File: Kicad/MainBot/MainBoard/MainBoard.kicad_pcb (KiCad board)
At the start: 2 copper layers, 2 parts, among them U1 AZ1117-3.3, U2 Teensy3.6

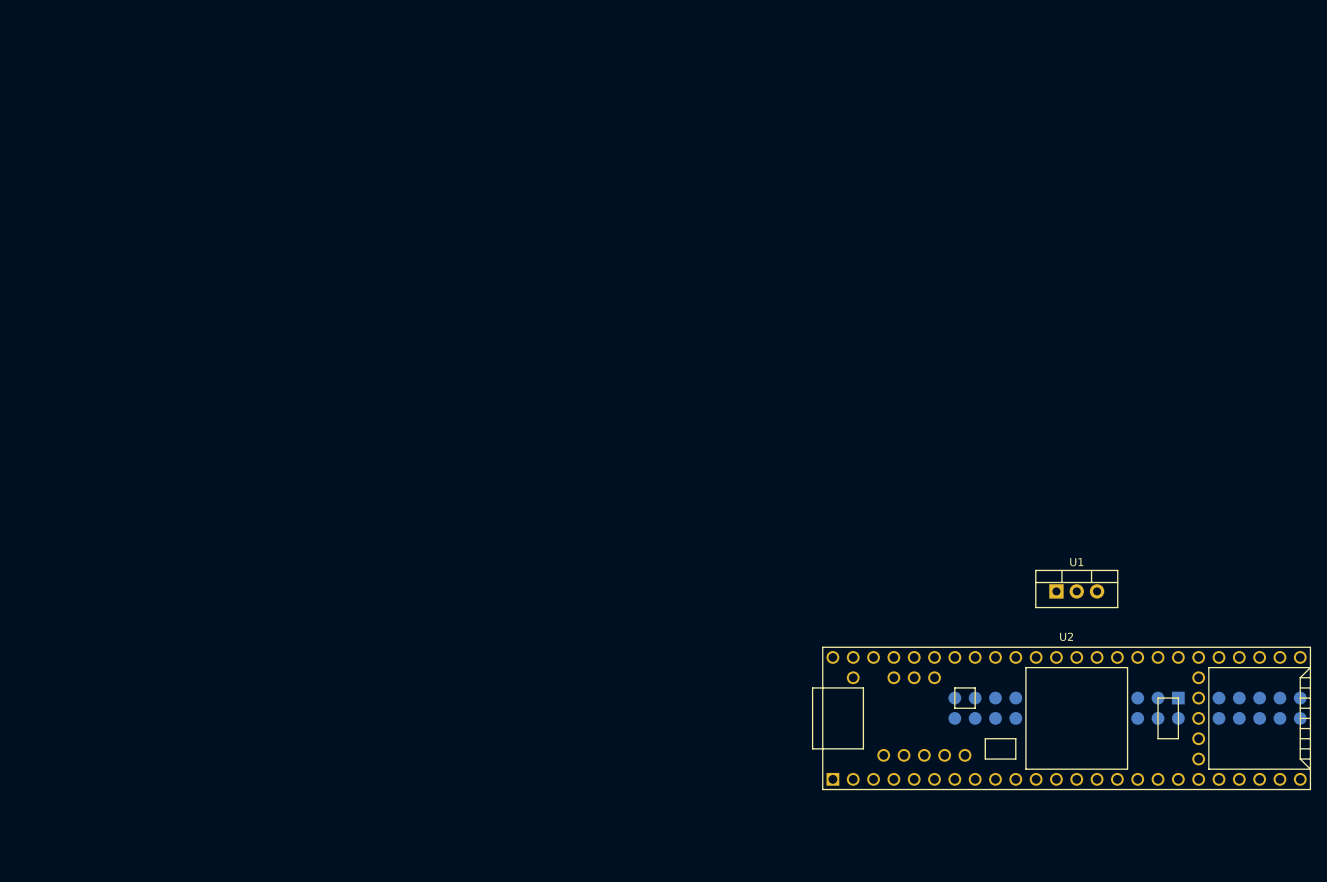
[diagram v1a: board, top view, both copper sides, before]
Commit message: Added multiplexer and driver footprint, updated PCB
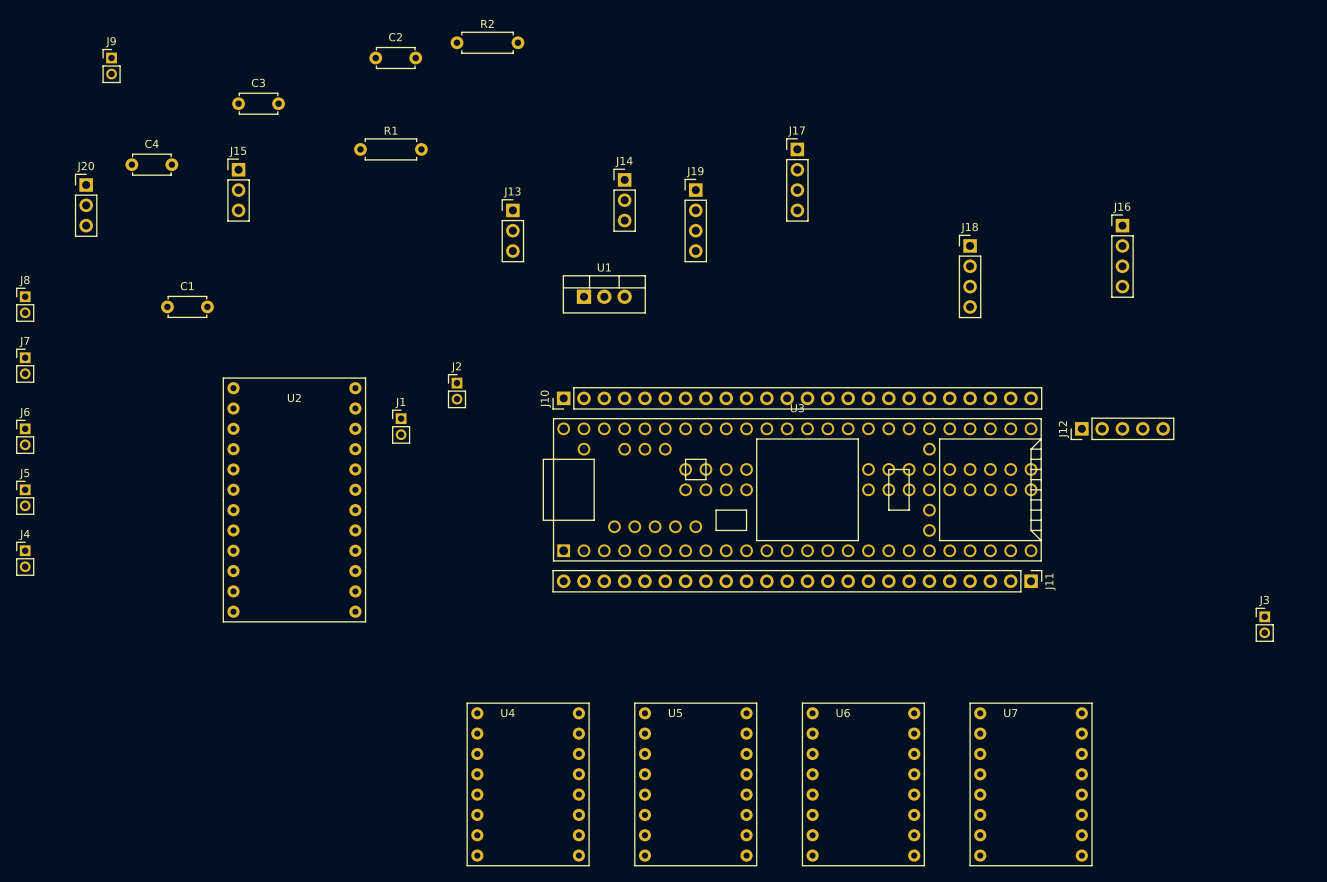
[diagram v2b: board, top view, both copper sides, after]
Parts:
- added C1: C, Capacitors_THT:C_Disc_D4.7mm_W2.5mm_P5.00mm, F.Cu at (35.6, 53.3)
- added C2: C, Capacitors_THT:C_Disc_D4.7mm_W2.5mm_P5.00mm, F.Cu at (61.6, 22.2)
- added C3: C, Capacitors_THT:C_Disc_D4.7mm_W2.5mm_P5.00mm, F.Cu at (44.5, 27.9)
- added C4: C, Capacitors_THT:C_Disc_D4.7mm_W2.5mm_P5.00mm, F.Cu at (31.1, 35.6)
- added J1: Conn_01x02, Pin_Headers:Pin_Header_Straight_1x02_Pitch2.00mm, F.Cu at (64.8, 67.3)
- added J10: Conn_01x24, Pin_Headers:Pin_Header_Straight_1x24_Pitch2.54mm, F.Cu at (85.1, 64.8)
- added J11: Conn_01x24, Pin_Headers:Pin_Header_Straight_1x24_Pitch2.54mm, F.Cu at (143.5, 87.6)
- added J12: Conn_01x05, Pin_Headers:Pin_Header_Straight_1x05_Pitch2.54mm, F.Cu at (149.9, 68.6)
- added J13: Conn_01x03, Pin_Headers:Pin_Header_Straight_1x03_Pitch2.54mm, F.Cu at (78.7, 41.3)
- added J14: Conn_01x03, Pin_Headers:Pin_Header_Straight_1x03_Pitch2.54mm, F.Cu at (92.7, 37.5)
- added J15: Conn_01x03, Pin_Headers:Pin_Header_Straight_1x03_Pitch2.54mm, F.Cu at (44.5, 36.2)
- added J16: Conn_01x04, Pin_Headers:Pin_Header_Straight_1x04_Pitch2.54mm, F.Cu at (154.9, 43.2)
- added J17: Conn_01x04, Pin_Headers:Pin_Header_Straight_1x04_Pitch2.54mm, F.Cu at (114.3, 33.7)
- added J18: Conn_01x04, Pin_Headers:Pin_Header_Straight_1x04_Pitch2.54mm, F.Cu at (135.9, 45.7)
- added J19: Conn_01x04, Pin_Headers:Pin_Header_Straight_1x04_Pitch2.54mm, F.Cu at (101.6, 38.7)
- added J2: Conn_01x02, Pin_Headers:Pin_Header_Straight_1x02_Pitch2.00mm, F.Cu at (71.8, 62.9)
- added J20: Conn_01x03, Pin_Headers:Pin_Header_Straight_1x03_Pitch2.54mm, F.Cu at (25.4, 38.1)
- added J3: Conn_01x02, Pin_Headers:Pin_Header_Straight_1x02_Pitch2.00mm, F.Cu at (172.7, 92.1)
- added J4: Conn_01x02, Pin_Headers:Pin_Header_Straight_1x02_Pitch2.00mm, F.Cu at (17.8, 83.8)
- added J5: Conn_01x02, Pin_Headers:Pin_Header_Straight_1x02_Pitch2.00mm, F.Cu at (17.8, 76.2)
- added J6: Conn_01x02, Pin_Headers:Pin_Header_Straight_1x02_Pitch2.00mm, F.Cu at (17.8, 68.6)
- added J7: Conn_01x02, Pin_Headers:Pin_Header_Straight_1x02_Pitch2.00mm, F.Cu at (17.8, 59.7)
- added J8: Conn_01x02, Pin_Headers:Pin_Header_Straight_1x02_Pitch2.00mm, F.Cu at (17.8, 52.1)
- added J9: Conn_01x02, Pin_Headers:Pin_Header_Straight_1x02_Pitch2.00mm, F.Cu at (28.6, 22.2)
- added R1: R, Resistors_THT:R_Axial_DIN0207_L6.3mm_D2.5mm_P7.62mm_Horizontal, F.Cu at (59.7, 33.7)
- added R2: R, Resistors_THT:R_Axial_DIN0207_L6.3mm_D2.5mm_P7.62mm_Horizontal, F.Cu at (71.8, 20.3)
- added U3: Teensy3.6, Teensy:Teensy35_36, F.Cu at (114.3, 76.2)
- added U4: DRV8825, Rex:DRV8825, F.Cu at (80.6, 113.0)
- added U5: DRV8825, Rex:DRV8825, F.Cu at (101.6, 113.0)
- added U6: DRV8825, Rex:DRV8825, F.Cu at (122.6, 113.0)
- added U7: DRV8825, Rex:DRV8825, F.Cu at (143.5, 113.0)
- U2: value Teensy3.6 -> TCA9548A; footprint Teensy:Teensy35_36 -> Rex:TCA9548A
- moved U2 112.0 mm to (43.8, 63.5)
- moved U1 69.6 mm to (87.6, 52.1)
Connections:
- U2 pad 1: GND -> (no net)
- U2 pad 10: Net-(U2-Pad10) -> (no net)
- U2 pad 11: Net-(U2-Pad11) -> (no net)
- U2 pad 12: Net-(U2-Pad12) -> (no net)
- U2 pad 13: Net-(U2-Pad13) -> (no net)
- U2 pad 14: Net-(U2-Pad14) -> (no net)
- U2 pad 15: Net-(U2-Pad15) -> (no net)
- U2 pad 16: Net-(U2-Pad16) -> (no net)
- U2 pad 17: Net-(U2-Pad17) -> (no net)
- U2 pad 18: Net-(U2-Pad18) -> (no net)
- U2 pad 19: Net-(U2-Pad19) -> (no net)
- U2 pad 2: Net-(U2-Pad2) -> (no net)
- U2 pad 20: Net-(U2-Pad20) -> (no net)
- U2 pad 21: Net-(U2-Pad21) -> (no net)
- U2 pad 22: Net-(U2-Pad22) -> (no net)
- U2 pad 23: Net-(U2-Pad23) -> (no net)
- U2 pad 24: Net-(U2-Pad24) -> (no net)
- U2 pad 3: Net-(U2-Pad3) -> (no net)
- U2 pad 4: /PWM_1 -> (no net)
- U2 pad 5: /PWM_2 -> (no net)
- U2 pad 6: /PWM_3 -> (no net)
- U2 pad 7: /PWM_4 -> (no net)
- U2 pad 8: Net-(U2-Pad8) -> (no net)
- U2 pad 9: Net-(U2-Pad9) -> (no net)

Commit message: Corrections and started PCB
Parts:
- added C10: 10µF, Capacitors_SMD:CP_Elec_8x5.4, F.Cu at (74.0, 136.8)
- added C11: 10µF, Capacitors_SMD:CP_Elec_8x5.4, F.Cu at (85.4, 136.8)
- added C12: 10µF, Capacitors_SMD:CP_Elec_8x5.4, F.Cu at (85.4, 126.0)
- added C13: 100µF, Capacitors_THT:CP_Radial_D6.3mm_P2.50mm, F.Cu at (200.7, 134.6)
- added C14: 100µF, Capacitors_THT:CP_Radial_D6.3mm_P2.50mm, F.Cu at (246.4, 135.9)
- added C15: 100µF, Capacitors_THT:CP_Radial_D6.3mm_P2.50mm, F.Cu at (273.1, 135.9)
- added C16: 100µF, Capacitors_THT:CP_Radial_D6.3mm_P2.50mm, F.Cu at (224.8, 134.6)
- added C5: 27pF, Capacitors_SMD:C_1206_HandSoldering, F.Cu at (123.2, 43.2)
- added C6: 10µF, Capacitors_SMD:CP_Elec_8x5.4, F.Cu at (74.0, 158.4)
- added C7: 10µF, Capacitors_SMD:CP_Elec_8x5.4, F.Cu at (85.4, 147.6)
- added C8: 10µF, Capacitors_SMD:CP_Elec_8x5.4, F.Cu at (85.4, 158.4)
- added C9: 10µF, Capacitors_SMD:CP_Elec_8x5.4, F.Cu at (74.0, 147.6)
- added D1: LED, LEDs:LED_1206, F.Cu at (162.6, 86.4)
- added D2: LED, LEDs:LED_1206, F.Cu at (162.6, 91.4)
- added D3: LED, LEDs:LED_1206, F.Cu at (162.6, 96.5)
- added J21: Conn_01x03, Pin_Headers:Pin_Header_Straight_1x03_Pitch2.54mm, F.Cu at (166.4, 133.3)
- added J22: Conn_01x03, Pin_Headers:Pin_Header_Straight_1x03_Pitch2.54mm, F.Cu at (172.7, 110.5)
- added J23: 01x04, Pin_Headers:Pin_Header_Straight_1x04_Pitch2.54mm, F.Cu at (217.2, 63.5)
- added J24: 01x03, Pin_Headers:Pin_Header_Straight_1x03_Pitch2.54mm, F.Cu at (177.8, 110.5)
- added J25: Conn_01x04, Pin_Headers:Pin_Header_Straight_1x04_Pitch2.54mm, F.Cu at (166.4, 120.7)
- added J26: 01x04, Pin_Headers:Pin_Header_Straight_1x04_Pitch2.54mm, F.Cu at (163.8, 24.1)
- added J27: Conn_01x02, Pin_Headers:Pin_Header_Straight_1x02_Pitch2.54mm, F.Cu at (172.7, 102.9)
- added J28: Conn_02x03_Counter_Clockwise, Pin_Headers:Pin_Header_Straight_2x03_Pitch2.54mm, F.Cu at (174.0, 133.3)
- added J29: Conn_02x03_Counter_Clockwise, Pin_Headers:Pin_Header_Straight_2x03_Pitch2.54mm, F.Cu at (161.3, 52.1)
- added J30: Conn_02x03_Counter_Clockwise, Pin_Headers:Pin_Header_Straight_2x03_Pitch2.54mm, F.Cu at (146.1, 133.3)
- added J31: Conn_02x03_Counter_Clockwise, Pin_Headers:Pin_Header_Straight_2x03_Pitch2.54mm, F.Cu at (153.7, 133.3)
- added J32: Conn_01x03, Connectors_JST:JST_XH_B03B-XH-A_03x2.50mm_Straight, F.Cu at (145.5, 112.8)
- added J33: Conn_01x03, Connectors_JST:JST_XH_B03B-XH-A_03x2.50mm_Straight, F.Cu at (146.1, 88.4)
- added J34: Conn_01x02, Pin_Headers:Pin_Header_Straight_1x02_Pitch2.54mm, F.Cu at (177.8, 102.9)
- added J35: Conn_01x02, Pin_Headers:Pin_Header_Straight_1x02_Pitch2.54mm, F.Cu at (182.9, 102.9)
- added J36: Conn_01x02, Pin_Headers:Pin_Header_Straight_1x02_Pitch2.54mm, F.Cu at (188.0, 102.9)
- added J37: Conn_01x02, Pin_Headers:Pin_Header_Straight_1x02_Pitch2.54mm, F.Cu at (157.5, 102.9)
- added J38: Conn_01x03, Connectors_JST:JST_XH_B03B-XH-A_03x2.50mm_Straight, F.Cu at (145.8, 96.5)
- added J39: Conn_01x04, Connectors_JST:JST_XH_B04B-XH-A_04x2.50mm_Straight, F.Cu at (232.4, 154.9)
- added J40: Conn_01x03, Connectors_JST:JST_XH_B03B-XH-A_03x2.50mm_Straight, F.Cu at (145.8, 104.6)
- added J41: 01x04, Connectors_JST:JST_XH_B04B-XH-A_04x2.50mm_Straight, F.Cu at (196.8, 146.1)
- added J42: 01x04, Connectors_JST:JST_XH_B04B-XH-A_04x2.50mm_Straight, F.Cu at (221.0, 144.8)
- added J43: 01x04, Connectors_JST:JST_XH_B04B-XH-A_04x2.50mm_Straight, F.Cu at (242.6, 144.8)
- added J44: 01x04, Connectors_JST:JST_XH_B04B-XH-A_04x2.50mm_Straight, F.Cu at (269.2, 144.8)
- added L1: 22µH, Rex:L1, F.Cu at (93.7, 129.9)
- added Q1: Q_PMOS_DGS, TO_SOT_Packages_SMD:SOT-23, F.Cu at (103.8, 152.7)
- added R10: 2.55k, Resistors_SMD:R_0805_HandSoldering, F.Cu at (15.9, 62.9)
- added R11: 2.55k, Resistors_SMD:R_0805_HandSoldering, F.Cu at (25.4, 65.4)
- added R12: 2.55k, Resistors_SMD:R_0805_HandSoldering, F.Cu at (15.2, 48.3)
- added R13: 2.55k, Resistors_SMD:R_0805_HandSoldering, F.Cu at (25.4, 50.8)
- added R14: 2.55k, Resistors_SMD:R_0805_HandSoldering, F.Cu at (15.2, 33.7)
- added R15: 2.55k, Resistors_SMD:R_0805_HandSoldering, F.Cu at (25.4, 36.2)
- added R16: 2.55k, Resistors_SMD:R_0805_HandSoldering, F.Cu at (15.2, 19.1)
- added R17: 2.55k, Resistors_SMD:R_0805_HandSoldering, F.Cu at (25.4, 21.6)
- added R18: 2.55k, Resistors_SMD:R_0805_HandSoldering, F.Cu at (57.1, 47.6)
- added R19: 2.55k, Resistors_SMD:R_0805_HandSoldering, F.Cu at (57.1, 45.7)
- added R20: 100k, Resistors_SMD:R_1206_HandSoldering, F.Cu at (57.8, 43.2)
- added R21: 100k, Resistors_SMD:R_1206_HandSoldering, F.Cu at (97.5, 148.3)
- added R22: 100k, Resistors_SMD:R_1206_HandSoldering, F.Cu at (103.2, 156.5)
- added R23: 100k, Resistors_SMD:R_1206_HandSoldering, F.Cu at (93.0, 159.7)
- added R24: 22.1k, Resistors_SMD:R_1206_HandSoldering, F.Cu at (93.0, 152.7)
- added R25: 2k, Resistors_SMD:R_1206_HandSoldering, F.Cu at (82.5, 111.8)
- added R26: 2k, Resistors_SMD:R_1206_HandSoldering, F.Cu at (82.5, 106.7)
- added R3: 2.55k, Resistors_SMD:R_0805_HandSoldering, F.Cu at (41.3, 65.4)
- added R4: 2.55k, Resistors_SMD:R_0805_HandSoldering, F.Cu at (41.3, 50.8)
- added R5: 2.55k, Resistors_SMD:R_0805_HandSoldering, F.Cu at (31.1, 48.3)
- added R6: 2.55k, Resistors_SMD:R_0805_HandSoldering, F.Cu at (31.1, 33.7)
- added R7: 2.55k, Resistors_SMD:R_0805_HandSoldering, F.Cu at (41.3, 36.2)
- added R8: 2.55k, Resistors_SMD:R_0805_HandSoldering, F.Cu at (31.1, 19.1)
- added R9: 2.55k, Resistors_SMD:R_0805_HandSoldering, F.Cu at (41.3, 22.2)
- C1, C3: value C -> 100nF; footprint Capacitors_THT:C_Disc_D4.7mm_W2.5mm_P5.00mm -> Capacitors_SMD:C_1206_HandSoldering
- C2: value C -> 4.7µF; footprint Capacitors_THT:C_Disc_D4.7mm_W2.5mm_P5.00mm -> Capacitors_SMD:C_1206_HandSoldering
- C4: value C -> 1µF; footprint Capacitors_THT:C_Disc_D4.7mm_W2.5mm_P5.00mm -> Capacitors_SMD:C_1206_HandSoldering
- J1, J2, J3, J4, J8, J9: value Conn_01x02 -> Conn_01x04; footprint Pin_Headers:Pin_Header_Straight_1x02_Pitch2.00mm -> Connectors_JST:JST_XH_B04B-XH-A_04x2.50mm_Straight
- J10, J11: value Conn_01x24 -> Conn_01x04; footprint Pin_Headers:Pin_Header_Straight_1x24_Pitch2.54mm -> Connectors_JST:JST_XH_B04B-XH-A_04x2.50mm_Straight
- J12: value Conn_01x05 -> Conn_01x04; footprint Pin_Headers:Pin_Header_Straight_1x05_Pitch2.54mm -> Connectors_JST:JST_XH_B04B-XH-A_04x2.50mm_Straight
- J13: value Conn_01x03 -> 01x02_DAC; footprint Pin_Headers:Pin_Header_Straight_1x03_Pitch2.54mm -> Pin_Headers:Pin_Header_Straight_1x02_Pitch2.54mm
- J14: value Conn_01x03 -> 01x02; footprint Pin_Headers:Pin_Header_Straight_1x03_Pitch2.54mm -> Pin_Headers:Pin_Header_Straight_1x02_Pitch2.54mm
- J15: value Conn_01x03 -> Conn_01x24; footprint Pin_Headers:Pin_Header_Straight_1x03_Pitch2.54mm -> Socket_Strips:Socket_Strip_Straight_1x24_Pitch2.54mm
- J16: value Conn_01x04 -> Conn_01x24; footprint Pin_Headers:Pin_Header_Straight_1x04_Pitch2.54mm -> Socket_Strips:Socket_Strip_Straight_1x24_Pitch2.54mm
- J17, J18: value Conn_01x04 -> 01x24; footprint Pin_Headers:Pin_Header_Straight_1x04_Pitch2.54mm -> Socket_Strips:Socket_Strip_Straight_1x24_Pitch2.54mm
- J19: value Conn_01x04 -> 01x05; footprint Pin_Headers:Pin_Header_Straight_1x04_Pitch2.54mm -> Pin_Headers:Pin_Header_Straight_1x05_Pitch2.54mm
- J20: value Conn_01x03 -> 01x03
- J5: value Conn_01x02 -> 02x04_I2C; footprint Pin_Headers:Pin_Header_Straight_1x02_Pitch2.00mm -> Pin_Headers:Pin_Header_Straight_2x04_Pitch2.54mm
- J6, J7: value Conn_01x02 -> 02x03; footprint Pin_Headers:Pin_Header_Straight_1x02_Pitch2.00mm -> Pin_Headers:Pin_Header_Straight_2x03_Pitch2.54mm
- R1: value R -> 2k; footprint Resistors_THT:R_Axial_DIN0207_L6.3mm_D2.5mm_P7.62mm_Horizontal -> Resistors_SMD:R_1206_HandSoldering
- R2: value R -> 2.55k; footprint Resistors_THT:R_Axial_DIN0207_L6.3mm_D2.5mm_P7.62mm_Horizontal -> Resistors_SMD:R_0805_HandSoldering
- U1: value AZ1117-3.3 -> TCA9548A; footprint TO_SOT_Packages_THT:TO-220-3_Vertical -> Rex:TCA9548A_TSSOP
- U2: value TCA9548A -> ISL85410; footprint Rex:TCA9548A -> DFN-12_DE-M:DFN-12_DE-M
- moved J20 165.9 mm to (161.3, 133.3)
- moved J17 164.4 mm to (260.4, 109.2), turned to 270 degrees
- moved J15 162.2 mm to (201.9, 74.9), turned to 90 degrees
- moved J5 160.3 mm to (175.8, 49.3)
- moved J3 158.3 mm to (21.0, 47.0), turned to 270 degrees
- moved C4 139.6 mm to (97.5, 158.4), turned to 270 degrees
- moved J18 138.0 mm to (260.4, 105.4), turned to 270 degrees
- moved J7 136.1 mm to (153.7, 52.1)
- moved C3 132.8 mm to (103.2, 147.0), turned to 90 degrees
- moved U7 130.8 mm to (273.1, 130.8)
- moved J6 129.3 mm to (146.1, 52.1)
- moved C2 128.6 mm to (97.5, 145.7), turned to 180 degrees
- moved J11 127.5 mm to (36.8, 17.8)
- moved U6 125.1 mm to (246.4, 130.8)
- moved U5 124.5 mm to (224.8, 130.8)
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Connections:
- C1 pad 1: GND -> /A13
- C1 pad 2: Net-(C1-Pad2) -> GND
- C2 pad 1: GND -> +12C
- C2 pad 2: Net-(C2-Pad2) -> GND
- C3 pad 1: GND -> Net-(C3-Pad1)
- C4 pad 1: GND -> Net-(C4-Pad1)
- C4 pad 2: +12V -> GND
- J1 pad 1: /TX_1 -> VCC
- J1 pad 2: /RX_1 -> /M_SC0
- J10 pad 1: /Vin -> VCC
- J10 pad 2: /AGND -> /M_SC5
- J10 pad 3: VCC -> /M_SD5
- J10 pad 4: /PWM_15 -> GND
- J11 pad 1: Net-(J11-Pad1) -> VCC
- J11 pad 2: Net-(J11-Pad2) -> /M_SC4
- J11 pad 3: /PWM_11 -> /M_SD4
- J11 pad 4: /PWM_10 -> GND
- J12 pad 1: Net-(J12-Pad1) -> VCC
- J12 pad 2: Net-(J12-Pad2) -> /TX2
- J12 pad 3: GND -> /RX2
- J12 pad 4: Net-(J12-Pad4) -> GND
- J13 pad 1: /DC_DIR_1 -> /A21
- J13 pad 2: /DC_PWM_1 -> /A22
- J14 pad 1: /DC_DIR_2 -> +12C
- J14 pad 2: /DC_PWM_2 -> GND
- J15 pad 1: /DC_DIR_3 -> /Vin
- J15 pad 2: /DC_PWM_3 -> GND
- J15 pad 3: GND -> VCC
- J16 pad 1: Net-(J16-Pad1) -> /Vin
- J16 pad 2: Net-(J16-Pad2) -> GND
- J16 pad 3: Net-(J16-Pad3) -> VCC
- J16 pad 4: Net-(J16-Pad4) -> /A9
- J17 pad 1: Net-(J17-Pad1) -> /A13
- J17 pad 2: Net-(J17-Pad2) -> /A12
- J17 pad 3: Net-(J17-Pad3) -> /PWM_11
- J17 pad 4: Net-(J17-Pad4) -> /PWM_10
- J18 pad 1: Net-(J18-Pad1) -> /A13
- J18 pad 2: Net-(J18-Pad2) -> /A12
- J18 pad 3: Net-(J18-Pad3) -> /PWM_11
- J18 pad 4: Net-(J18-Pad4) -> /PWM_10
- J19 pad 3: Net-(J19-Pad3) -> GND
- J19 pad 4: Net-(J19-Pad4) -> VCC
- J2 pad 1: /M_SD0 -> VCC
- J2 pad 2: /M_SC0 -> /M_SC1
- J20 pad 1: /DC_DIR_4 -> Net-(J20-Pad1)
- J20 pad 2: /DC_PWM_4 -> Net-(J20-Pad2)
- J20 pad 3: GND -> Net-(J20-Pad3)
- J3 pad 1: /M_SD1 -> VCC
- J3 pad 2: /M_SC1 -> /M_SC2
- J4 pad 1: /M_SD2 -> VCC
- J4 pad 2: /M_SC2 -> /M_SC3
- J5 pad 1: /M_SD3 -> /A19
- J5 pad 2: /M_SC3 -> /SCA1
- J6 pad 1: /M_SD4 -> /MISO1
- J6 pad 2: /M_SC4 -> /A13
- J7 pad 1: /M_SD5 -> /MISO2
- J7 pad 2: /M_SC5 -> /SCK2
- J8 pad 1: /M_SD6 -> VCC
- J8 pad 2: /M_SC6 -> /M_SC7
- J9 pad 1: /M_SD7 -> VCC
- J9 pad 2: /M_SC7 -> /M_SC6
- R1 pad 1: /SDA1 -> VCC
- R1 pad 2: VCC -> Net-(D1-Pad2)
- R2 pad 1: /SCL1 -> VCC
- R2 pad 2: VCC -> /M_SC7
- U1 pad 1: GND -> VCC
- U1 pad 2: VCC -> GND
- U1 pad 3: +12V -> /A19
- U2 pad 1: (no net) -> Net-(C4-Pad1)
- U2 pad 10: (no net) -> Net-(C5-Pad2)
- U2 pad 11: (no net) -> Net-(C4-Pad1)
- U2 pad 12: (no net) -> Net-(C4-Pad1)
- U2 pad 13: (no net) -> GND
- U2 pad 2: (no net) -> Net-(R22-Pad1)
- U2 pad 3: (no net) -> Net-(C3-Pad1)
- U2 pad 4: (no net) -> +12C
- U2 pad 5: (no net) -> Net-(C3-Pad2)
- U2 pad 6: (no net) -> GND
- U2 pad 7: (no net) -> Net-(R21-Pad1)
- U2 pad 8: (no net) -> Net-(U2-Pad8)
- U2 pad 9: (no net) -> Net-(C4-Pad1)
- U3 pad 11: /PWM_8 -> /RX2
- U3 pad 12: /PWM_9 -> /TX2
- U3 pad 13: Net-(J11-Pad12) -> /MOSI0
- U3 pad 14: Net-(J11-Pad11) -> /MISO0
- U3 pad 16: Net-(J11-Pad9) -> /STEP_DIR_1
- U3 pad 17: Net-(J11-Pad8) -> /STEP_DIR_2
- U3 pad 18: Net-(J11-Pad7) -> /STEP_DIR_3
- U3 pad 19: Net-(J11-Pad6) -> /STEP_DIR_4
- U3 pad 2: /RX1 -> /MOSI1
- U3 pad 20: Net-(J11-Pad5) -> /STEP_STP_1
- U3 pad 23: Net-(J11-Pad2) -> /A12
- U3 pad 24: Net-(J11-Pad1) -> /A13
- U3 pad 25: Net-(J12-Pad5) -> Net-(J19-Pad5)
- U3 pad 26: Net-(J12-Pad4) -> VCC
- U3 pad 28: Net-(J12-Pad2) -> Net-(J19-Pad2)
- U3 pad 29: Net-(J12-Pad1) -> Net-(J19-Pad1)
- U3 pad 3: /TX1 -> /MISO1
- U3 pad 30: Net-(J10-Pad24) -> /A14
- U3 pad 31: Net-(J10-Pad23) -> /A15
- U3 pad 32: /PWM17 -> /A16
- U3 pad 33: /PWM16 -> /A17
- U3 pad 34: /SCL1 -> /A18
- U3 pad 35: /SDA1 -> /A19
- U3 pad 36: Net-(J10-Pad18) -> /A20
- U3 pad 37: Net-(J10-Pad17) -> /A21
- U3 pad 38: Net-(J10-Pad16) -> /A22
- U3 pad 4: /PWM_1 -> /DC_PWM_1
- U3 pad 40: Net-(J10-Pad14) -> Net-(J15-Pad14)
- U3 pad 41: Net-(J10-Pad13) -> /ADDR_0
- U3 pad 42: Net-(J10-Pad12) -> /ADDR_1
- U3 pad 43: Net-(J10-Pad11) -> /ADDR_2
- U3 pad 47: /PWM_12 -> /47
- U3 pad 48: /PWM_13 -> /A7
- U3 pad 49: /PWM_14 -> /A8
- U3 pad 5: /PWM_2 -> /DC_PWM_2
- U3 pad 50: /PWM_15 -> /A9
- U3 pad 52: /AGND -> GND
- U3 pad 53: /Vin -> Net-(J27-Pad1)
- U3 pad 55: Net-(U3-Pad55) -> /AREF
- U3 pad 56: Net-(U3-Pad56) -> /A10
- U3 pad 57: Net-(U3-Pad57) -> /A11
- U3 pad 6: /PWM_3 -> /DC_PWM_3
- U3 pad 61: Net-(U3-Pad61) -> GND
- U3 pad 62: Net-(U3-Pad62) -> GND
- U3 pad 67: Net-(U3-Pad67) -> /DEB_L_1
- U3 pad 68: Net-(U3-Pad68) -> /DEB_L_2
- U3 pad 7: /PWM_4 -> /DC_PWM_4
- U3 pad 71: Net-(U3-Pad71) -> /MOSI2
- U3 pad 72: Net-(U3-Pad72) -> /MISO2
- U3 pad 73: Net-(U3-Pad73) -> /SCK2
- U3 pad 78: Net-(U3-Pad78) -> /A23
- U3 pad 79: Net-(U3-Pad79) -> /A24
- U3 pad 80: Net-(U3-Pad80) -> Net-(J20-Pad3)
- U3 pad 81: Net-(U3-Pad81) -> Net-(J20-Pad2)
- U3 pad 82: Net-(U3-Pad82) -> Net-(J20-Pad1)
- U4 pad 1: (no net) -> /ENABLE_INV_1
- U4 pad 10: (no net) -> /FAU_1
- U4 pad 11: (no net) -> Net-(J41-Pad4)
- U4 pad 12: (no net) -> Net-(J41-Pad3)
- U4 pad 13: (no net) -> Net-(J41-Pad2)
- U4 pad 14: (no net) -> Net-(J41-Pad1)
- U4 pad 15: (no net) -> GND
- U4 pad 16: (no net) -> +12C
- U4 pad 2: (no net) -> /M0_1
- U4 pad 3: (no net) -> /M1_1
- U4 pad 4: (no net) -> /M2_1
- U4 pad 5: (no net) -> VCC
- U4 pad 6: (no net) -> VCC
- U4 pad 7: (no net) -> /STEP_STP_1
- U4 pad 8: (no net) -> /STEP_DIR_1
- U4 pad 9: (no net) -> GND
- U5 pad 1: (no net) -> /ENABLE_INV_2
- U5 pad 10: (no net) -> /FAU_2
- U5 pad 11: (no net) -> Net-(J42-Pad4)
- U5 pad 12: (no net) -> Net-(J42-Pad3)
- U5 pad 13: (no net) -> Net-(J42-Pad2)
- U5 pad 14: (no net) -> Net-(J42-Pad1)
- U5 pad 15: (no net) -> GND
- U5 pad 16: (no net) -> +12C
- U5 pad 2: (no net) -> /M0_2
- U5 pad 3: (no net) -> /M1_2
- U5 pad 4: (no net) -> /M2_2
- U5 pad 5: (no net) -> VCC
- U5 pad 6: (no net) -> VCC
- U5 pad 7: (no net) -> /PWM_10
- U5 pad 8: (no net) -> /STEP_DIR_2
- U5 pad 9: (no net) -> GND
- U6 pad 1: (no net) -> /ENABLE_INV_3
- U6 pad 10: (no net) -> /FAU_3
- U6 pad 11: (no net) -> Net-(J43-Pad4)
- U6 pad 12: (no net) -> Net-(J43-Pad3)
- U6 pad 13: (no net) -> Net-(J43-Pad2)
- U6 pad 14: (no net) -> Net-(J43-Pad1)
- U6 pad 15: (no net) -> GND
- U6 pad 16: (no net) -> +12C
- U6 pad 2: (no net) -> /M0_3
- U6 pad 3: (no net) -> /M1_3
- U6 pad 4: (no net) -> /M2_3
- U6 pad 5: (no net) -> VCC
- U6 pad 6: (no net) -> VCC
- U6 pad 7: (no net) -> /PWM_11
- U6 pad 8: (no net) -> /STEP_DIR_3
- U6 pad 9: (no net) -> GND
- U7 pad 1: (no net) -> /ENABLE_INV_4
- U7 pad 10: (no net) -> /FAU_4
- U7 pad 11: (no net) -> Net-(J44-Pad4)
- U7 pad 12: (no net) -> Net-(J44-Pad3)
- U7 pad 13: (no net) -> Net-(J44-Pad2)
- U7 pad 14: (no net) -> Net-(J44-Pad1)
- U7 pad 15: (no net) -> GND
- U7 pad 16: (no net) -> +12C
- U7 pad 2: (no net) -> /M0_4
- U7 pad 3: (no net) -> /M1_4
- U7 pad 4: (no net) -> /M2_4
- U7 pad 5: (no net) -> VCC
- U7 pad 6: (no net) -> VCC
- U7 pad 7: (no net) -> /A12
- U7 pad 8: (no net) -> /STEP_DIR_4
- U7 pad 9: (no net) -> GND
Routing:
- net VCC: track 0.00 -> 86.1 mm
- net /M_SC5: track 0.00 -> 5.76 mm
- net /M_SC1: track 0.00 -> 5.76 mm
- net /M_SC4: track 0.00 -> 5.76 mm
- net /M_SC2: track 0.00 -> 5.76 mm
- net /M_SC0: track 0.00 -> 5.76 mm
- net /M_SC3: track 0.00 -> 5.13 mm
- net /M_SD4: track 0.00 -> 4.77 mm
- net /M_SD1: track 0.00 -> 4.51 mm
- net /M_SD5: track 0.00 -> 4.51 mm
- net /M_SD0: track 0.00 -> 4.51 mm
- net /M_SD3: track 0.00 -> 4.51 mm
- net /M_SD2: track 0.00 -> 4.51 mm
- net (no net): track 0.00 -> 0.73 mm
- net Net-(C4-Pad1): track 0.00 -> 0.50 mm

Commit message: So much things :)
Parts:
- removed J27: Conn_01x02, Pin_Headers:Pin_Header_Straight_1x02_Pitch2.54mm
- moved J44 228.3 mm to (78.7, 19.1), turned to 180 degrees
- moved C15 225.0 mm to (74.9, 29.2), turned to 270 degrees
- moved U7 220.9 mm to (74.9, 33.0), turned to 180 degrees
- moved J43 189.8 mm to (100.3, 19.1), turned to 180 degrees
- moved C14 184.0 mm to (96.5, 29.2), turned to 270 degrees
- moved U6 178.9 mm to (96.5, 33.0), turned to 180 degrees
- moved J18 168.1 mm to (97.5, 63.5), turned to 0 degrees
- moved J17 164.7 mm to (102.1, 63.5), turned to 0 degrees
- moved J23 161.4 mm to (72.4, 134.9), turned to 180 degrees
- moved J42 160.1 mm to (121.9, 19.1), turned to 180 degrees
- moved C16 150.0 mm to (118.1, 29.2), turned to 270 degrees
- moved U3 146.3 mm to (84.8, 92.7), turned to 90 degrees
- moved U5 144.7 mm to (118.1, 33.0), turned to 180 degrees
- moved J16 143.6 mm to (67.6, 121.9), turned to 180 degrees
- moved J41 138.9 mm to (143.5, 17.8), turned to 180 degrees
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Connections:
- U3 pad 53: Net-(J27-Pad1) -> /Vin
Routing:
- net /STEP_STP_1: track 0.00 -> 101.1 mm, vias 0 -> 2
- net /PWM_10: track 0.00 -> 78.1 mm
- net +12C: track 0.00 -> 72.1 mm
- net /M_SC3: track 5.13 -> 72.2 mm
- net /A12: track 0.00 -> 62.2 mm
- net /M_SD3: track 4.51 -> 64.8 mm, vias 0 -> 2
- net /PWM_11: track 0.00 -> 58.2 mm
- net /M_SC0: track 5.76 -> 59.7 mm, vias 0 -> 2
- net /M_SD0: track 4.51 -> 48.9 mm, vias 0 -> 2
- net /M_SC2: track 5.76 -> 47.9 mm, vias 0 -> 2
- net /M_SC1: track 5.76 -> 44.0 mm, vias 0 -> 2
- net /M_SC7: track 0.00 -> 36.5 mm
- net /M_SD1: track 4.51 -> 40.8 mm, vias 0 -> 2
- net /M_SD6: track 0.00 -> 35.9 mm
- net VCC: track 86.1 -> 118.4 mm
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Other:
- net class 2 added: clearance 0.4, trace_width 0.75, via_dia 0.6, via_drill 0.4
- net class Default: trace_width 0.25 -> 0.6

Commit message: ??
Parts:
- moved J32 82.7 mm to (33.8, 145.7), turned to 0 degrees
- moved J33 74.6 mm to (46.0, 145.7), turned to 0 degrees
- moved J38 70.0 mm to (58.2, 145.7), turned to 0 degrees
- moved J40 69.4 mm to (70.4, 145.7), turned to 0 degrees
- moved J5 54.9 mm to (73.4, 43.2)
- moved J41 26.9 mm to (158.5, 40.0)
- moved J12 26.7 mm to (129.4, 112.4), turned to 270 degrees
- moved J14 26.0 mm to (30.0, 129.5), turned to 0 degrees
- moved D2 25.8 mm to (69.9, 80.4)
- moved Q1 25.8 mm to (69.0, 128.5)
- moved R24 25.8 mm to (58.2, 128.5)
- moved C16 25.8 mm to (133.1, 50.2)
- moved U5 25.8 mm to (133.1, 54.0)
- moved C1 25.8 mm to (76.7, 59.2)
- moved D1 25.8 mm to (64.8, 103.3)
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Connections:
- J5 pad 2: /SCA1 -> /A18
- J5 pad 7: /SCA1 -> /A18
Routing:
- net +12C: track 72.1 -> 449.2 mm, vias 0 -> 5
- net GND: track 0.00 -> 117.8 mm, vias 0 -> 10
- net /STEP_DIR_1: track 0.00 -> 117.4 mm, vias 0 -> 1
- net VCC: track 118.4 -> 234.1 mm, vias 0 -> 12
- net /A13: track 11.2 -> 109.8 mm
- net /DC_PWM_1: track 0.00 -> 92.9 mm
- net /A19: track 8.24 -> 98.7 mm, vias 0 -> 1
- net /STEP_DIR_2: track 0.00 -> 89.1 mm, vias 0 -> 3
- net /A18: track 7.74 -> 94.3 mm, vias 0 -> 1
- net /DC_PWM_2: track 0.00 -> 82.2 mm
- net /STEP_DIR_3: track 0.00 -> 82.2 mm, vias 0 -> 9
- net /44: track 0.00 -> 80.6 mm
- net /STEP_DIR_4: track 0.00 -> 80.6 mm, vias 0 -> 3
- net /DEB_L_1: track 0.00 -> 79.7 mm
- net /ADDR_0: track 11.0 -> 83.6 mm
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- added copper zone on In2.Cu, net GND
- added copper zone on VccPlane.Cu, net VCC
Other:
- copper layers 2 -> 4

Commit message: ?
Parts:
- added G***: LOGO, Logo:logo, F.Cu at (156.6, 113.0)
- added R27: 910kR, Resistors_SMD:R_1206_HandSoldering, F.Cu at (85.0, 74.0)
- added R28: 100kR, Resistors_SMD:R_1206_HandSoldering, F.Cu at (85.0, 78.0)
- added REF**: MountingHole_4.3mm_M4_ISO7380, Mounting_Holes:MountingHole_4.3mm_M4_ISO7380, F.Cu at (25.0, 157.0)
- added REF**: MountingHole_4.3mm_M4_ISO7380, Mounting_Holes:MountingHole_4.3mm_M4_ISO7380, F.Cu at (171.0, 35.0)
- added REF**: MountingHole_4.3mm_M4_ISO7380, Mounting_Holes:MountingHole_4.3mm_M4_ISO7380, F.Cu at (171.0, 157.0)
- added REF**: MountingHole_4.3mm_M4_ISO7380, Mounting_Holes:MountingHole_4.3mm_M4_ISO7380, F.Cu at (25.0, 35.0)
- J14: footprint Pin_Headers:Pin_Header_Straight_1x02_Pitch2.54mm -> Rex:BatConn
- moved J14 68.3 mm to (92.0, 158.0), turned to 180 degrees
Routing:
- net /A20: track 14.7 -> 61.8 mm, vias 0 -> 4
- net +12C: track 449.2 -> 464.8 mm
- net GND: track 117.8 -> 119.8 mm, vias 10 -> 11
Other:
- board outline added: 158 x 134 mm
- board text added: "14/03/2019"
- board text added: "A2 A1 B1 B2"
- board text added: "BAT+|BAT-"
- board text added: "DIR PWM GND"
- board text added: "E"
- board text added: "ENABLE"
- board text added: "For RTS"
- board text added: "GND SD SC VCC"
- board text added: "M2 M1 M0"
- board text added: "MainBot Motherboard by Arnaud Schlumberger"
- board text added: "PWR_LED"
- board text added: "SCK GND VCC SDA"
- board text added: "o"
